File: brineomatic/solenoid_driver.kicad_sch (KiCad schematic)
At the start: 11 parts, among them J7 3.5MM, J8 3.5MM, Q1 Si2318

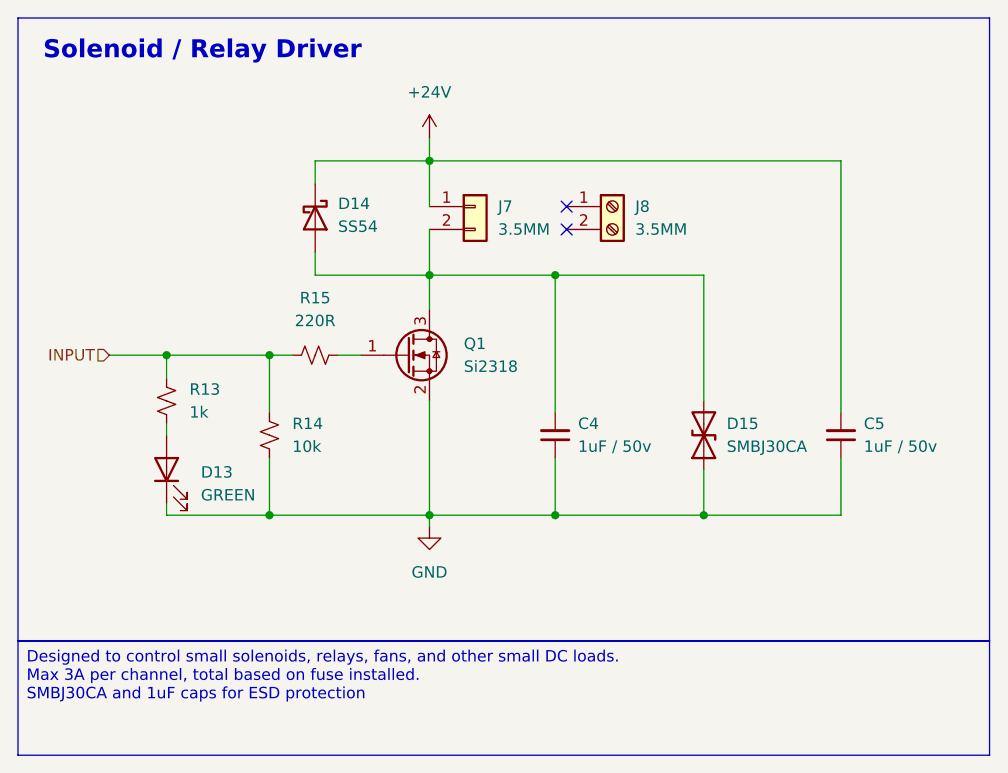
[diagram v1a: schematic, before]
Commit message: added 1uF cap to pressure sensor connectors for esd
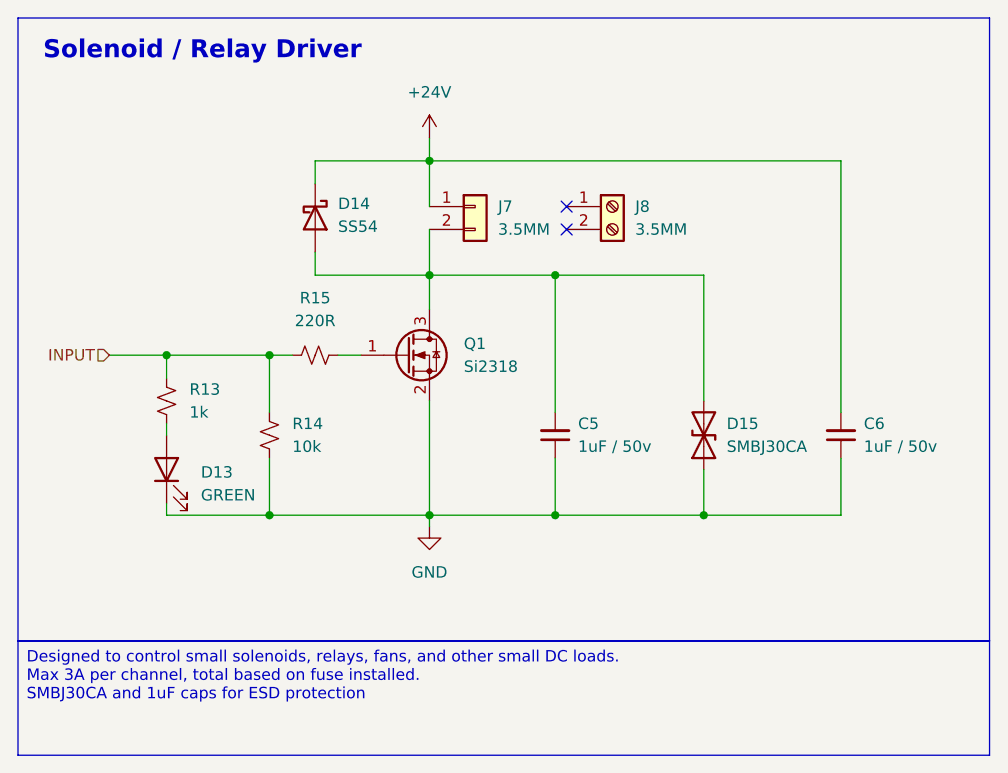
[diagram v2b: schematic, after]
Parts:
- renumbered C4 to C5, C5 to C6
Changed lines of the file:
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@@
 		(dnp no)
 		(fields_autoplaced yes)
-		(property "Reference" "C4"
+		(property "Reference" "C5"
 			(at 154.94 96.5135 0)
 			(effects
@@
 			(project "brineomatic"
 				(path "/96477ae2-ef08-48f3-8dd4-fe4478541f68/427089b2-03f8-442f-beb9-df87f2c31083"
-					(reference "C25")
+					(reference "C26")
 					(unit 1)
 				)
 				(path "/96477ae2-ef08-48f3-8dd4-fe4478541f68/53b9b350-c996-44b6-8dbf-2a99841f1965"
-					(reference "C54")
+					(reference "C56")
 					(unit 1)
 				)
 				(path "/96477ae2-ef08-48f3-8dd4-fe4478541f68/91db2587-0f96-4292-982e-c9eb44a28398"
-					(reference "C4")
+					(reference "C5")
 					(unit 1)
 				)
 				(path "/96477ae2-ef08-48f3-8dd4-fe4478541f68/c855463c-7233-4758-aee4-aa81e2b08bc2"
-					(reference "C23")
+					(reference "C24")
 					(unit 1)
 				)
 				(path "/96477ae2-ef08-48f3-8dd4-fe4478541f68/dbb171ac-9e75-41dd-9596-6fac72a797a4"
-					(reference "C27")
+					(reference "C28")
 					(unit 1)
 				)
@@
 		(on_board yes)
 		(dnp no)
-		(property "Reference" "C5"
+		(property "Reference" "C6"
 			(at 186.69 96.5135 0)
 			(effects
@@
 			(project "brineomatic"
 				(path "/96477ae2-ef08-48f3-8dd4-fe4478541f68/427089b2-03f8-442f-beb9-df87f2c31083"
-					(reference "C26")
+					(reference "C27")
 					(unit 1)
 				)
 				(path "/96477ae2-ef08-48f3-8dd4-fe4478541f68/53b9b350-c996-44b6-8dbf-2a99841f1965"
-					(reference "C55")
+					(reference "C57")
 					(unit 1)
 				)
 				(path "/96477ae2-ef08-48f3-8dd4-fe4478541f68/91db2587-0f96-4292-982e-c9eb44a28398"
-					(reference "C5")
+					(reference "C6")
 					(unit 1)
 				)
 				(path "/96477ae2-ef08-48f3-8dd4-fe4478541f68/c855463c-7233-4758-aee4-aa81e2b08bc2"
-					(reference "C24")
+					(reference "C25")
 					(unit 1)
 				)
 				(path "/96477ae2-ef08-48f3-8dd4-fe4478541f68/dbb171ac-9e75-41dd-9596-6fac72a797a4"
-					(reference "C28")
-					(unit 1)
-				)
+					(reference "C29")
+					(unit 1)
+				)

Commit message: holy re-routing batman. board is fully routed first pass.
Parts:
- renumbered C5 to C6, C6 to C7
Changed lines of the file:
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@@
 				)
 				(path "/96477ae2-ef08-48f3-8dd4-fe4478541f68/53b9b350-c996-44b6-8dbf-2a99841f1965"
-					(reference "D48")
+					(reference "D47")
 					(unit 1)
 				)
@@
 		(dnp no)
 		(fields_autoplaced yes)
-		(property "Reference" "C5"
+		(property "Reference" "C6"
 			(at 154.94 96.5135 0)
 			(effects
@@
 			(project "brineomatic"
 				(path "/96477ae2-ef08-48f3-8dd4-fe4478541f68/427089b2-03f8-442f-beb9-df87f2c31083"
-					(reference "C26")
-					(unit 1)
-				)
-				(path "/96477ae2-ef08-48f3-8dd4-fe4478541f68/53b9b350-c996-44b6-8dbf-2a99841f1965"
-					(reference "C56")
+					(reference "C27")
+					(unit 1)
+				)
+				(path "/96477ae2-ef08-48f3-8dd4-fe4478541f68/53b9b350-c996-44b6-8dbf-2a99841f1965"
+					(reference "C61")
 					(unit 1)
 				)
 				(path "/96477ae2-ef08-48f3-8dd4-fe4478541f68/91db2587-0f96-4292-982e-c9eb44a28398"
-					(reference "C5")
+					(reference "C6")
 					(unit 1)
 				)
 				(path "/96477ae2-ef08-48f3-8dd4-fe4478541f68/c855463c-7233-4758-aee4-aa81e2b08bc2"
-					(reference "C24")
+					(reference "C25")
 					(unit 1)
 				)
 				(path "/96477ae2-ef08-48f3-8dd4-fe4478541f68/dbb171ac-9e75-41dd-9596-6fac72a797a4"
-					(reference "C28")
+					(reference "C29")
 					(unit 1)
 				)
@@
 				)
 				(path "/96477ae2-ef08-48f3-8dd4-fe4478541f68/53b9b350-c996-44b6-8dbf-2a99841f1965"
-					(reference "D49")
+					(reference "D48")
 					(unit 1)
 				)
@@
 		(on_board yes)
 		(dnp no)
-		(property "Reference" "C6"
+		(property "Reference" "C7"
 			(at 186.69 96.5135 0)
 			(effects
@@
 			(project "brineomatic"
 				(path "/96477ae2-ef08-48f3-8dd4-fe4478541f68/427089b2-03f8-442f-beb9-df87f2c31083"
-					(reference "C27")
-					(unit 1)
-				)
-				(path "/96477ae2-ef08-48f3-8dd4-fe4478541f68/53b9b350-c996-44b6-8dbf-2a99841f1965"
-					(reference "C57")
+					(reference "C28")
+					(unit 1)
+				)
+				(path "/96477ae2-ef08-48f3-8dd4-fe4478541f68/53b9b350-c996-44b6-8dbf-2a99841f1965"
+					(reference "C62")
 					(unit 1)
 				)
 				(path "/96477ae2-ef08-48f3-8dd4-fe4478541f68/91db2587-0f96-4292-982e-c9eb44a28398"
-					(reference "C6")
+					(reference "C7")
 					(unit 1)
 				)
 				(path "/96477ae2-ef08-48f3-8dd4-fe4478541f68/c855463c-7233-4758-aee4-aa81e2b08bc2"
-					(reference "C25")
+					(reference "C26")
 					(unit 1)
 				)
 				(path "/96477ae2-ef08-48f3-8dd4-fe4478541f68/dbb171ac-9e75-41dd-9596-6fac72a797a4"
-					(reference "C29")
+					(reference "C30")
 					(unit 1)
 				)
@@
 				)
 				(path "/96477ae2-ef08-48f3-8dd4-fe4478541f68/53b9b350-c996-44b6-8dbf-2a99841f1965"
-					(reference "D47")
-					(unit 1)
-				)
+					(reference "D46")
+					(unit 1)
+				)

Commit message: added test points
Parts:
- added TP8, TP9: TestPoint, TestPoint:TestPoint_Pad_D1.5mm, symbol Connector:TestPoint
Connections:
- net +24V: now also TP8.1
- net at C6.2, D14.2 (A), D15.2 (A2)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: now also TP9.1
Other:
- moved on the sheet: D14
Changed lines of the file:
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@@
+	)
+	(junction
+		(at 130.81 80.01)
+		(diameter 0)
+		(color 0 0 0 0)
 	)
 	(junction
@@
 	)
 	(junction
+		(at 130.81 67.31)
+		(diameter 0)
+		(color 0 0 0 0)
+	)
+	(junction
 		(at 138.43 106.68)
 		(diameter 0)
@@
 	(wire
 		(pts
-			(xy 125.73 80.01) (xy 125.73 77.47)
+			(xy 115.57 80.01) (xy 115.57 77.47)
 		)
 		(stroke
@@
 	(wire
 		(pts
-			(xy 125.73 80.01) (xy 138.43 80.01)
+			(xy 115.57 80.01) (xy 130.81 80.01)
 		)
 		(stroke
@@
 	(wire
 		(pts
-			(xy 125.73 67.31) (xy 125.73 69.85)
+			(xy 115.57 67.31) (xy 115.57 69.85)
 		)
 		(stroke
@@
 	(wire
 		(pts
+			(xy 130.81 80.01) (xy 138.43 80.01)
+		)
+		(stroke
+			(width 0)
+			(type default)
+		)
+	)
+	(wire
+		(pts
 			(xy 138.43 64.77) (xy 138.43 67.31)
 		)
@@
 	(wire
 		(pts
+			(xy 130.81 67.31) (xy 115.57 67.31)
+		)
+		(stroke
+			(width 0)
+			(type default)
+		)
+	)
+	(wire
+		(pts
 			(xy 138.43 93.98) (xy 138.43 106.68)
 		)
@@
 	(wire
 		(pts
-			(xy 138.43 67.31) (xy 125.73 67.31)
+			(xy 138.43 67.31) (xy 130.81 67.31)
 		)
 		(stroke
@@
 	(symbol
 		(lib_id "Device:D_Schottky")
-		(at 125.73 73.66 270)
+		(at 115.57 73.66 270)
 		(unit 1)
 		(exclude_from_sim no)
@@
 		(fields_autoplaced yes)
 		(property "Reference" "D14"
-			(at 128.27 72.0724 90)
+			(at 118.11 72.0724 90)
 			(effects
 				(font
@@
 		)
 		(property "Value" "SS54"
-			(at 128.27 74.6124 90)
+			(at 118.11 74.6124 90)
 			(effects
 				(font
@@
 		)
 		(property "Footprint" "Diode_SMD:D_SMA"
-			(at 121.285 73.66 0)
+			(at 111.125 73.66 0)
 			(effects
 				(font
@@
 		)
 		(property "Datasheet" ""
-			(at 125.73 73.66 0)
+			(at 115.57 73.66 0)
 			(effects
 				(font
@@
 		)
 		(property "Description" ""
-			(at 125.73 73.66 0)
+			(at 115.57 73.66 0)
 			(effects
 				(font
@@
 		)
 		(property "Sim.Device" "D"
-			(at 125.73 73.66 0)
+			(at 115.57 73.66 0)
 			(effects
 				(font
@@
 		)
 		(property "Sim.Pins" "1=K 2=A"
-			(at 125.73 73.66 0)
+			(at 115.57 73.66 0)
 			(effects
 				(font
@@
 		)
 		(property "Mouser" ""
-			(at 125.73 73.66 0)
+			(at 115.57 73.66 0)
 			(effects
 				(font
@@
 		)
 		(property "LCSC" "C22452"
-			(at 125.73 73.66 0)
+			(at 115.57 73.66 0)
 			(effects
 				(font
@@
 	)
 	(symbol
+		(lib_id "Connector:TestPoint")
+		(at 130.81 67.31 180)
+		(unit 1)
+		(exclude_from_sim no)
+		(in_bom yes)
+		(on_board yes)
+		(dnp no)
+		(property "Reference" "TP8"
+			(at 132.08 72.39 0)
+			(effects
+				(font
+					(size 1.27 1.27)
+				)
+				(justify left)
+			)
+		)
+		(property "Value" "TestPoint"
+			(at 128.27 69.3421 0)
+			(effects
+				(font
+					(size 1.27 1.27)
+				)
+				(justify left)
+				(hide yes)
+			)
+		)
+		(property "Footprint" "TestPoint:TestPoint_Pad_D1.5mm"
+			(at 125.73 67.31 0)
+			(effects
+				(font
+					(size 1.27 1.27)
+				)
+				(hide yes)
+			)
+		)
+		(property "Datasheet" "~"
+			(at 125.73 67.31 0)
+			(effects
+				(font
+					(size 1.27 1.27)
+				)
+				(hide yes)
+			)
+		)
+		(property "Description" "test point"
+			(at 130.81 67.31 0)
+			(effects
+				(font
+					(size 1.27 1.27)
+				)
+				(hide yes)
+			)
+		)
+		(pin "1"
+		)
+		(instances
+			(project "brineomatic"
+				(path "/96477ae2-ef08-48f3-8dd4-fe4478541f68/427089b2-03f8-442f-beb9-df87f2c31083"
+					(reference "TP20")
+					(unit 1)
+				)
+				(path "/96477ae2-ef08-48f3-8dd4-fe4478541f68/53b9b350-c996-44b6-8dbf-2a99841f1965"
+					(reference "TP36")
+					(unit 1)
+				)
+				(path "/96477ae2-ef08-48f3-8dd4-fe4478541f68/91db2587-0f96-4292-982e-c9eb44a28398"
+					(reference "TP8")
+					(unit 1)
+				)
+				(path "/96477ae2-ef08-48f3-8dd4-fe4478541f68/c855463c-7233-4758-aee4-aa81e2b08bc2"
+					(reference "TP18")
+					(unit 1)
+				)
+				(path "/96477ae2-ef08-48f3-8dd4-fe4478541f68/dbb171ac-9e75-41dd-9596-6fac72a797a4"
+					(reference "TP22")
+					(unit 1)
+				)
+			)
+		)
+	)
+	(symbol
 		(lib_id "Device:C_Small")
 		(at 152.4 97.79 180)
@@
 					(unit 1)
 				)
+			)
+		)
+	)
+	(symbol
+		(lib_id "Connector:TestPoint")
+		(at 130.81 80.01 0)
+		(unit 1)
+		(exclude_from_sim no)
+		(in_bom yes)
+		(on_board yes)
+		(dnp no)
+		(property "Reference" "TP9"
+			(at 129.54 74.93 0)
+			(effects
+				(font
+					(size 1.27 1.27)
+				)
+				(justify left)
+			)
+		)
+		(property "Value" "TestPoint"
+			(at 133.35 77.9779 0)
+			(effects
+				(font
+					(size 1.27 1.27)
+				)
+				(justify left)
+				(hide yes)
+			)
+		)
+		(property "Footprint" "TestPoint:TestPoint_Pad_D1.5mm"
+			(at 135.89 80.01 0)
+			(effects
+				(font
+					(size 1.27 1.27)
+				)
+				(hide yes)
+			)
+		)
+		(property "Datasheet" "~"
+			(at 135.89 80.01 0)
+			(effects
+				(font
+					(size 1.27 1.27)
+				)
+				(hide yes)
+			)
+		)
+		(property "Description" "test point"
+			(at 130.81 80.01 0)
+			(effects
+				(font
+					(size 1.27 1.27)
+				)
+				(hide yes)
+			)
+		)
+		(pin "1"
+		)
+		(instances
+			(project "brineomatic"
+				(path "/96477ae2-ef08-48f3-8dd4-fe4478541f68/427089b2-03f8-442f-beb9-df87f2c31083"
+					(reference "TP21")
+					(unit 1)
+				)
+				(path "/96477ae2-ef08-48f3-8dd4-fe4478541f68/53b9b350-c996-44b6-8dbf-2a99841f1965"
+					(reference "TP37")
+					(unit 1)
+				)
+				(path "/96477ae2-ef08-48f3-8dd4-fe4478541f68/91db2587-0f96-4292-982e-c9eb44a28398"
+					(reference "TP9")
+					(unit 1)
+				)
+				(path "/96477ae2-ef08-48f3-8dd4-fe4478541f68/c855463c-7233-4758-aee4-aa81e2b08bc2"
+					(reference "TP19")
+					(unit 1)
+				)
+				(path "/96477ae2-ef08-48f3-8dd4-fe4478541f68/dbb171ac-9e75-41dd-9596-6fac72a797a4"
+					(reference "TP23")
+					(unit 1)
+				)

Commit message: removed LC filter and various cleanup for rev c
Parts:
- removed TP8: TestPoint, TestPoint:TestPoint_Pad_D1.5mm, symbol Connector:TestPoint
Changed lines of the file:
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@@
-	)
-	(junction
-		(at 130.81 67.31)
-		(diameter 0)
-		(color 0 0 0 0)
 	)
 	(junction
@@
 	(wire
 		(pts
-			(xy 130.81 67.31) (xy 115.57 67.31)
+			(xy 115.57 67.31) (xy 138.43 67.31)
 		)
 		(stroke
@@
 		(pts
 			(xy 168.91 106.68) (xy 168.91 101.6)
-		)
-		(stroke
-			(width 0)
-			(type default)
-		)
-	)
-	(wire
-		(pts
-			(xy 138.43 67.31) (xy 130.81 67.31)
 		)
 		(stroke
@@
 					(unit 1)
 				)
-			)
-		)
-	)
-	(symbol
-		(lib_id "Connector:TestPoint")
-		(at 130.81 67.31 180)
-		(unit 1)
-		(exclude_from_sim no)
-		(in_bom yes)
-		(on_board yes)
-		(dnp no)
-		(property "Reference" "TP8"
-			(at 132.08 72.39 0)
-			(effects
-				(font
-					(size 1.27 1.27)
-				)
-				(justify left)
-			)
-		)
-		(property "Value" "TestPoint"
-			(at 128.27 69.3421 0)
-			(effects
-				(font
-					(size 1.27 1.27)
-				)
-				(justify left)
-				(hide yes)
-			)
-		)
-		(property "Footprint" "TestPoint:TestPoint_Pad_D1.5mm"
-			(at 125.73 67.31 0)
-			(effects
-				(font
-					(size 1.27 1.27)
-				)
-				(hide yes)
-			)
-		)
-		(property "Datasheet" "~"
-			(at 125.73 67.31 0)
-			(effects
-				(font
-					(size 1.27 1.27)
-				)
-				(hide yes)
-			)
-		)
-		(property "Description" "test point"
-			(at 130.81 67.31 0)
-			(effects
-				(font
-					(size 1.27 1.27)
-				)
-				(hide yes)
-			)
-		)
-		(pin "1"
-		)
-		(instances
-			(project "brineomatic"
-				(path "/96477ae2-ef08-48f3-8dd4-fe4478541f68/427089b2-03f8-442f-beb9-df87f2c31083"
-					(reference "TP20")
-					(unit 1)
-				)
-				(path "/96477ae2-ef08-48f3-8dd4-fe4478541f68/53b9b350-c996-44b6-8dbf-2a99841f1965"
-					(reference "TP36")
-					(unit 1)
-				)
-				(path "/96477ae2-ef08-48f3-8dd4-fe4478541f68/91db2587-0f96-4292-982e-c9eb44a28398"
-					(reference "TP8")
-					(unit 1)
-				)
-				(path "/96477ae2-ef08-48f3-8dd4-fe4478541f68/c855463c-7233-4758-aee4-aa81e2b08bc2"
-					(reference "TP18")
-					(unit 1)
-				)
-				(path "/96477ae2-ef08-48f3-8dd4-fe4478541f68/dbb171ac-9e75-41dd-9596-6fac72a797a4"
-					(reference "TP22")
-					(unit 1)
-				)

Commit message: bom and placement verified
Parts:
- C6, C7: value 1uF / 50v -> 1uF; LCSC (none) -> C15849
- D15: LCSC (none) -> C83847
- TP9: now left out of the parts list
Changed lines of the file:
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@@
 			)
 		)
-		(property "Value" "1uF / 50v"
+		(property "Value" "1uF"
 			(at 154.94 99.0535 0)
 			(effects
@@
 		)
 		(property "Supplier Part" ""
+			(at 152.4 97.79 0)
+			(effects
+				(font
+					(size 1.27 1.27)
+				)
+				(hide yes)
+			)
+		)
+		(property "LCSC" "C15849"
 			(at 152.4 97.79 0)
 			(effects
@@
 			)
 		)
-		(property "LCSC" ""
+		(property "LCSC" "C83847"
 			(at 168.91 97.79 90)
 			(effects
@@
 			)
 		)
-		(property "Value" "1uF  / 50v"
+		(property "Value" "1uF"
 			(at 186.69 99.0535 0)
 			(effects
@@
 		)
 		(property "Supplier Part" ""
+			(at 184.15 97.79 0)
+			(effects
+				(font
+					(size 1.27 1.27)
+				)
+				(hide yes)
+			)
+		)
+		(property "LCSC" "C15849"
 			(at 184.15 97.79 0)
 			(effects
@@
 		(unit 1)
 		(exclude_from_sim no)
-		(in_bom yes)
+		(in_bom no)
 		(on_board yes)
 		(dnp no)
